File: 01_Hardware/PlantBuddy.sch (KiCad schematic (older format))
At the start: 68 parts, among them J1 SWD, Q1 AO3401, Q2 FS8205, Q3 FS8205, U1 CN301, U2 INA138, U3 LMC555xM, U4 XC6206P332MR, U5 BlueNRG-M1, U6 SHT20, U7 CN3063, U8 DW01+G, Y1 16MHz, Y2 32kHz

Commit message: PCB almost done
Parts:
- renumbered Q2 to Q3
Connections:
- net VCC: no longer C1.1, Q1.3 (D), R8.1, U3.4 (R), U3.8 (VCC)
- new net Vhum: C1.1, Q1.3 (D), R8.1, U3.4 (R), U3.8 (VCC)
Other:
- note added: "98_Other/PCB-Considerations.jpg"
- note removed: "pic/PCB-Considerations.jpg"
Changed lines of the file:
@@
 $EndComp
 Connection ~ 3675 2100
-$Comp
-L power:VCC #PWR05
-U 1 1 5F79DB75
-P 1675 1700
-F 0 "#PWR05" H 1675 1550 50  0001 C CNN
-F 1 "VCC" H 1690 1873 50  0000 C CNN
-F 2 "" H 1675 1700 50  0001 C CNN
-F 3 "" H 1675 1700 50  0001 C CNN
-	1    1675 1700
-	1    0    0    -1
-$EndComp
 Text Label 3550 1900 2    50   ~ 0
 fHumidity
@@
 Wire Wire Line
 	1675 1700 1900 1700
-Connection ~ 1675 1700
 $Comp
 L power:GND #PWR06
@@
 $EndComp
 Connection ~ 900  1000
-$Comp
-L power:VCC #PWR07
-U 1 1 5F7A3D8C
-P 1700 1000
-F 0 "#PWR07" H 1700 850 50  0001 C CNN
-F 1 "VCC" H 1715 1173 50  0000 C CNN
-F 2 "" H 1700 1000 50  0001 C CNN
-F 3 "" H 1700 1000 50  0001 C CNN
-	1    1700 1000
-	1    0    0    -1
-$EndComp
 Wire Wire Line
 	1700 1000 1500 1000
@@
 Special layout considerations:
 Text Notes 6475 775  0    50   ~ 10
-pic/PCB-Considerations.jpg
+98_Other/PCB-Considerations.jpg
 $Comp
 L Device:Antenna_Shield AE1
@@
 U 1 1 5F7C98A8
 P 5775 4325
-F 0 "R13" H 5625 4375 50  0000 L CNN
+F 0 "R13" H 5575 4375 50  0000 L CNN
 F 1 "10k" H 5575 4275 50  0000 L CNN
 F 2 "Resistor_SMD:R_0603_1608Metric" H 5775 4325 50  0001 C CNN
@@
 $EndComp
 $Comp
-L PidgeonRepeller:Q_DUAL_NMOS_FS8205 Q2
+L PidgeonRepeller:Q_DUAL_NMOS_FS8205 Q3
 U 2 1 5F8AAEF8
 P 9975 6150
-F 0 "Q2" V 10224 6150 50  0000 C CNN
+F 0 "Q3" V 10224 6150 50  0000 C CNN
 F 1 "FS8205" V 10315 6150 50  0000 C CNN
 F 2 "Package_TO_SOT_SMD:SOT-23-6" H 10175 6150 50  0001 C CNN
@@
 	2    9975 6150
 	0    1    1    0
-$EndComp
-$Comp
-L PidgeonRepeller:Q_DUAL_NMOS_FS8205 Q3
-U 1 1 5F8AC644
-P 10375 6150
-F 0 "Q3" V 10624 6150 50  0000 C CNN
-F 1 "FS8205" V 10715 6150 50  0000 C CNN
-F 2 "Package_TO_SOT_SMD:SOT-23-6" H 10575 6150 50  0001 C CNN
-F 3 "~" H 10575 6150 50  0001 C CNN
-F 4 "C32254" H 10375 6150 50  0001 C CNN "LCSC"
-	1    10375 6150
-	0    -1   1    0
 $EndComp
 Wire Wire Line
@@
 Text Notes 7800 3350 0    26   ~ 0
 RoT: ~~0.3pF per PAD
+$Comp
+L PidgeonRepeller:Q_DUAL_NMOS_FS8205 Q3
+U 1 1 5F8AC644
+P 10375 6150
+F 0 "Q3" V 10624 6150 50  0000 C CNN
+F 1 "FS8205" V 10715 6150 50  0000 C CNN
+F 2 "Package_TO_SOT_SMD:SOT-23-6" H 10575 6150 50  0001 C CNN
+F 3 "~" H 10575 6150 50  0001 C CNN
+F 4 "C32254" H 10375 6150 50  0001 C CNN "LCSC"
+	1    10375 6150
+	0    -1   1    0
+$EndComp
+Text Label 1700 1000 2    50   ~ 0
+Vhum
+Text Label 1675 1700 0    50   ~ 0
+Vhum
 $EndSCHEMATC

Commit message: Initial Layout done
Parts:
- removed C16: 100nF, Capacitor_SMD:C_0603_1608Metric, symbol Device:C_Small
- SC1: footprint TestPoint:TestPoint_2Pads_Pitch5.08mm_Drill1.3mm -> PlantBuddy:SolarCell
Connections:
- no-connect marks 5 -> 6
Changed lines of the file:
@@
 F 0 "SC1" H 1008 4621 50  0000 L CNN
 F 1 "Solar_Cell" H 1008 4530 50  0000 L CNN
-F 2 "TestPoint:TestPoint_2Pads_Pitch5.08mm_Drill1.3mm" V 900 4585 50  0001 C CNN
+F 2 "PlantBuddy:SolarCell" V 900 4585 50  0001 C CNN
 F 3 "~" V 900 4585 50  0001 C CNN
 	1    900  4525
@@
 NoConn ~ 5775 3725
 $Comp
-L Device:C_Small C16
-U 1 1 5FA07683
-P 7325 4275
-F 0 "C16" H 7450 4325 50  0000 L CNN
-F 1 "100nF" H 7425 4250 50  0000 L CNN
-F 2 "Capacitor_SMD:C_0603_1608Metric" H 7325 4275 50  0001 C CNN
-F 3 "~" H 7325 4275 50  0001 C CNN
-F 4 "C14663" H 7325 4275 50  0001 C CNN "LCSC"
-	1    7325 4275
-	1    0    0    -1
-$EndComp
-$Comp
 L Device:C_Small C9
 U 1 1 5FA07E6E
@@
 	1    0    0    -1
 $EndComp
-Wire Wire Line
-	7325 4425 7125 4425
-Connection ~ 7125 4425
-Wire Wire Line
-	7125 4125 7325 4125
-Wire Wire Line
-	7325 4425 7325 4375
-Wire Wire Line
-	7325 4175 7325 4125
 NoConn ~ 7125 4025
 Wire Wire Line
@@
 Text Label 1675 1700 0    50   ~ 0
 Vhum
+NoConn ~ 7125 4125
 $EndSCHEMATC

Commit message: Ordered PCB
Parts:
- C26: value 22pF -> 20pF; LCSC C1555 -> C1554
- D2: LCSC C72043 -> C2286
- L3: LCSC C27124 -> C77122
- R16: value 160R -> 1k; LCSC C22814 -> C21190
- R8: value Ra -> 330k; LCSC (none) -> C17629
- R9: value Rb -> 330k; LCSC (none) -> C17629
- U6: value SHT20 -> SHT21; LCSC C53865 -> C84828
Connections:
- net VCC: now also U2.4 (-); no longer U2.3 (+)
- net VPanel: now also U2.3 (+); no longer U2.4 (-)
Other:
- note added: "N3: Avoid debugging this circuit w/o battery connected."
- note added: "eN5: With 330k we get a nice \n~~1.4MHz signal for 1pF\nand a 1kHz signal at 1nF"
- note removed: "Footprint TBD"
- note removed: "N3: Never debug this circuit w/o battery connected."
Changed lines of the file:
@@
 P 3675 2200
 F 0 "R9" H 3734 2246 50  0000 L CNN
-F 1 "Rb" H 3734 2155 50  0000 L CNN
+F 1 "330k" H 3734 2155 50  0000 L CNN
 F 2 "Resistor_SMD:R_0805_2012Metric" H 3675 2200 50  0001 C CNN
 F 3 "~" H 3675 2200 50  0001 C CNN
+F 4 "C17629" H 3675 2200 50  0001 C CNN "LCSC"
 	1    3675 2200
 	1    0    0    -1
@@
 P 3675 2000
 F 0 "R8" H 3734 2046 50  0000 L CNN
-F 1 "Ra" H 3734 1955 50  0000 L CNN
+F 1 "330k" H 3734 1955 50  0000 L CNN
 F 2 "Resistor_SMD:R_0805_2012Metric" H 3675 2000 50  0001 C CNN
 F 3 "~" H 3675 2000 50  0001 C CNN
+F 4 "C17629" H 3675 2000 50  0001 C CNN "LCSC"
 	1    3675 2000
 	1    0    0    -1
@@
 P 6925 1400
 F 0 "U6" H 6750 1825 50  0000 C CNN
-F 1 "SHT20" H 6825 1750 50  0000 C CNN
+F 1 "SHT21" H 6825 1750 50  0000 C CNN
 F 2 "Package_DFN_QFN:DFN-6-1EP_3x3mm_P1mm_EP1.5x2.4mm" H 6925 1400 50  0001 C CNN
 F 3 "https://datasheet.lcsc.com/szlcsc/Sensirion-SHT20_C53865.pdf" H 6925 1400 50  0001 C CNN
-F 4 "C53865" H 6925 1400 50  0001 C CNN "LCSC"
+F 4 "C84828" H 6925 1400 50  0001 C CNN "LCSC"
 	1    6925 1400
 	1    0    0    -1
@@
 F 4 "C47914" V 2050 4350 50  0001 C CNN "LCSC"
 	1    2050 4350
-	0    1    1    0
+	0    -1   1    0
 $EndComp
 $Comp
@@
 	-1   0    0    1
 $EndComp
-Wire Wire Line
-	2050 4850 1750 4850
 Connection ~ 2050 4850
 Wire Wire Line
@@
 Wire Wire Line
 	900  4050 900  4325
-Wire Wire Line
-	1750 4250 1750 4850
 Wire Wire Line
 	2050 4650 2500 4650
@@
 L power:+3.3V #PWR08
 U 1 1 5F81D2F2
-P 2350 4250
-F 0 "#PWR08" H 2350 4100 50  0001 C CNN
-F 1 "+3.3V" H 2475 4350 50  0000 C CNN
-F 2 "" H 2350 4250 50  0001 C CNN
-F 3 "" H 2350 4250 50  0001 C CNN
-	1    2350 4250
-	1    0    0    -1
+P 1750 4250
+F 0 "#PWR08" H 1750 4100 50  0001 C CNN
+F 1 "+3.3V" H 1875 4350 50  0000 C CNN
+F 2 "" H 1750 4250 50  0001 C CNN
+F 3 "" H 1750 4250 50  0001 C CNN
+	1    1750 4250
+	-1   0    0    -1
 $EndComp
 Text Notes 2375 3975 0    50   ~ 0
@@
 U 1 1 5F88B2CB
 P 7775 5875
-F 0 "R17" H 7716 5921 50  0000 R CNN
-F 1 "120k" H 7716 5830 50  0000 R CNN
+F 0 "R17" H 7750 5925 50  0000 R CNN
+F 1 "120k" H 7750 5825 50  0000 R CNN
 F 2 "Resistor_SMD:R_0603_1608Metric" H 7775 5875 50  0001 C CNN
 F 3 "~" H 7775 5875 50  0001 C CNN
@@
 Wire Wire Line
 	7125 3225 7525 3225
-Text Notes 4300 2400 0    50   ~ 0
-Footprint TBD
 Wire Wire Line
 	9100 4875 9100 5400
@@
 	1    0    0    -1
 $EndComp
-Wire Wire Line
-	1750 4850 900  4850
-Connection ~ 1750 4850
 Connection ~ 900  4850
 $Comp
@@
 $EndComp
 Text Notes 7050 6725 0    50   ~ 0
-N3: Never debug this circuit w/o battery connected.
+N3: Avoid debugging this circuit w/o battery connected.
 $Comp
 L Device:D_Schottky_Small D1
@@
 F 2 "LED_SMD:LED_0603_1608Metric" V 7650 3800 50  0001 C CNN
 F 3 "~" V 7650 3800 50  0001 C CNN
-F 4 "C72043" V 7650 3800 50  0001 C CNN "LCSC"
+F 4 "C2286" V 7650 3800 50  0001 C CNN "LCSC"
 	1    7650 3800
 	0    -1   -1   0
@@
 P 7650 3600
 F 0 "R16" V 7454 3600 50  0000 C CNN
-F 1 "160R" V 7545 3600 50  0000 C CNN
+F 1 "1k" V 7545 3600 50  0000 C CNN
 F 2 "Resistor_SMD:R_0603_1608Metric" H 7650 3600 50  0001 C CNN
 F 3 "~" H 7650 3600 50  0001 C CNN
-F 4 "C22814" V 7650 3600 50  0001 C CNN "LCSC"
+F 4 "C21190" V 7650 3600 50  0001 C CNN "LCSC"
 	1    7650 3600
 	-1   0    0    1
@@
 F 2 "Inductor_SMD:L_0402_1005Metric" H 9075 2775 50  0001 C CNN
 F 3 "~" H 9075 2775 50  0001 C CNN
-F 4 "C27124" H 9075 2775 50  0001 C CNN "LCSC"
+F 4 "C77122" H 9075 2775 50  0001 C CNN "LCSC"
 	1    9075 2775
 	0    -1   -1   0
@@
 P 9550 2775
 F 0 "C26" V 9350 2850 50  0000 R CNN
-F 1 "22pF" V 9425 2875 50  0000 R CNN
+F 1 "20pF" V 9425 2875 50  0000 R CNN
 F 2 "Capacitor_SMD:C_0402_1005Metric" H 9550 2775 50  0001 C CNN
 F 3 "~" H 9550 2775 50  0001 C CNN
-F 4 "C1555" H 9550 2775 50  0001 C CNN "LCSC"
+F 4 "C1554" H 9550 2775 50  0001 C CNN "LCSC"
 	1    9550 2775
 	0    1    1    0
@@
 Vhum
 NoConn ~ 7125 4125
+Text Notes 3975 2175 0    50   ~ 0
+eN5: With 330k we get a nice \n~~1.4MHz signal for 1pF\nand a 1kHz signal at 1nF
+Wire Wire Line
+	900  4850 2050 4850
+$Comp
+L power:GND #PWR0101
+U 1 1 5F89C24C
+P 2350 4250
+F 0 "#PWR0101" H 2350 4000 50  0001 C CNN
+F 1 "GND" H 2355 4077 50  0000 C CNN
+F 2 "" H 2350 4250 50  0001 C CNN
+F 3 "" H 2350 4250 50  0001 C CNN
+	1    2350 4250
+	1    0    0    -1
+$EndComp
 $EndSCHEMATC

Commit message: Evrika! We have an LED blinking! 🔥🎉💯
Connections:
- net +3V3: now also U5.27 (SMPSFILT2)
- no-connect marks 6 -> 5
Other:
- note added: "E1: The maximum output swing is Vss - 1V = 2.3V\nwhich is equivalent to a current of ~~24mA.\nWe need to lower the gain by choosing\nanother resistor value. Say 330k. Do this in\nthe next iteration & solder manually at home"
- note added: "N5: !WE NEED! SMPSFILT2\nto be connected to VCC"
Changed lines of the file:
@@
 Text Label 1675 1700 0    50   ~ 0
 Vhum
-NoConn ~ 7125 4125
 Text Notes 3975 2175 0    50   ~ 0
 eN5: With 330k we get a nice \n~~1.4MHz signal for 1pF\nand a 1kHz signal at 1nF
@@
 	1    0    0    -1
 $EndComp
+Text Notes 1375 5425 0    50   ~ 0
+E1: The maximum output swing is Vss - 1V = 2.3V\nwhich is equivalent to a current of ~~24mA.\nWe need to lower the gain by choosing\nanother resistor value. Say 330k. Do this in\nthe next iteration & solder manually at home
+$Comp
+L power:+3.3V #PWR?
+U 1 1 5FA2857E
+P 7375 4125
+F 0 "#PWR?" H 7375 3975 50  0001 C CNN
+F 1 "+3.3V" H 7390 4298 50  0000 C CNN
+F 2 "" H 7375 4125 50  0001 C CNN
+F 3 "" H 7375 4125 50  0001 C CNN
+	1    7375 4125
+	1    0    0    -1
+$EndComp
+Wire Wire Line
+	7375 4125 7125 4125
+Text Notes 7300 4325 0    50   ~ 10
+N5: !WE NEED! SMPSFILT2\nto be connected to VCC
 $EndSCHEMATC

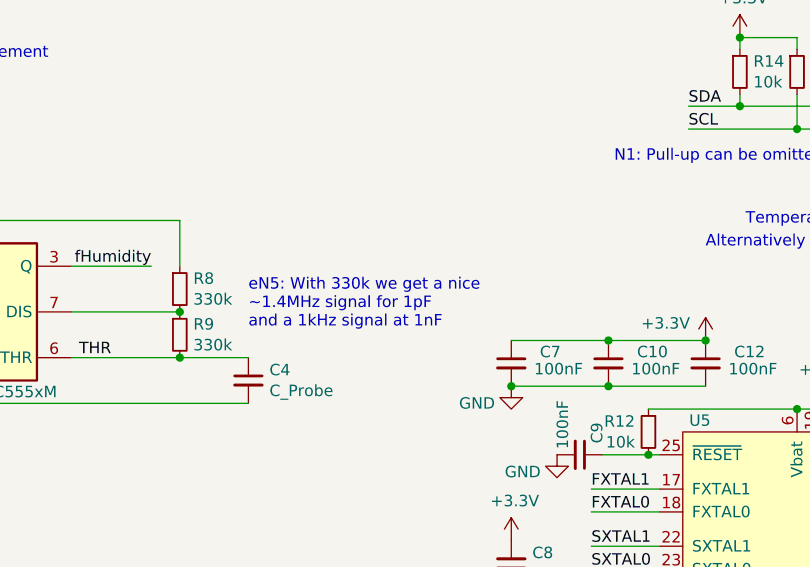
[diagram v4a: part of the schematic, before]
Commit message: Just some small typo fix.
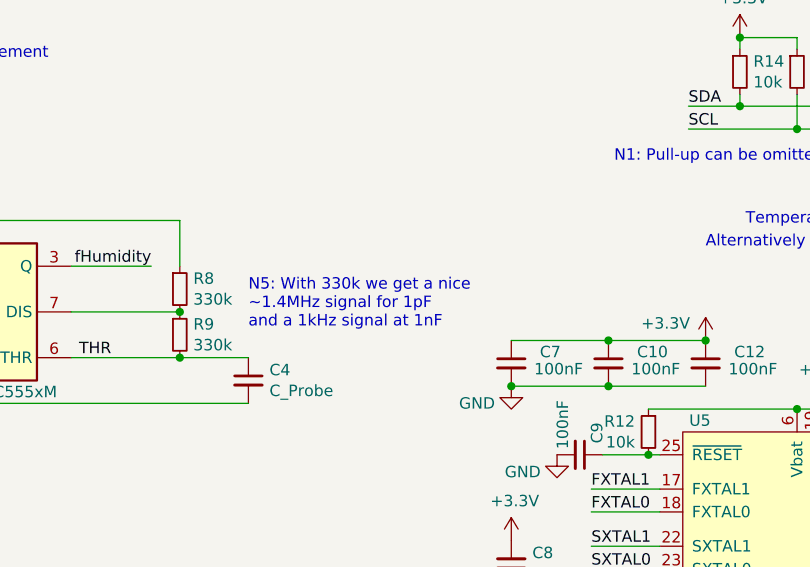
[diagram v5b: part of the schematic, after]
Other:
- note added: "N5: With 330k we get a nice \n~~1.4MHz signal for 1pF\nand a 1kHz signal at 1nF"
- note removed: "eN5: With 330k we get a nice \n~~1.4MHz signal for 1pF\nand a 1kHz signal at 1nF"
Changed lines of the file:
@@
 Vhum
 Text Notes 3975 2175 0    50   ~ 0
-eN5: With 330k we get a nice \n~~1.4MHz signal for 1pF\nand a 1kHz signal at 1nF
+N5: With 330k we get a nice \n~~1.4MHz signal for 1pF\nand a 1kHz signal at 1nF
 Wire Wire Line
 	900  4850 2050 4850

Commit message: Started schematic revision
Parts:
- removed BT1: Li+, Battery:BatteryHolder_Keystone_1060_1x2032, symbol Device:Battery_Cell
- removed C17, C21, C25: 22uF, Capacitor_SMD:C_0603_1608Metric, symbol Device:C_Small
- removed C24: 100nF, Capacitor_SMD:C_0603_1608Metric, symbol Device:C_Small
- removed C3, C5: 2.2uF, Capacitor_SMD:C_0603_1608Metric, symbol Device:C_Small
- removed D1, D3: B5819W, Diode_SMD:D_SOD-123, symbol Device:D_Schottky_Small
- removed Q2, Q3: FS8205, Package_TO_SOT_SMD:SOT-23-6, symbol PidgeonRepeller:Q_DUAL_NMOS_FS8205
- removed R1, R3, R4: 1M, Resistor_SMD:R_0603_1608Metric, symbol Device:R_Small
- removed R10, R11, R17: 120k, Resistor_SMD:R_0603_1608Metric, symbol Device:R_Small
- removed R18: 160R, Resistor_SMD:R_0603_1608Metric, symbol Device:R_Small
- removed R19, R7: 10k, Resistor_SMD:R_0603_1608Metric, symbol Device:R_Small
- removed R5: 1R0, Resistor_SMD:R_0603_1608Metric, symbol Device:R_Small
- removed R6: 470k, Resistor_SMD:R_0603_1608Metric, symbol Device:R_Small
- removed SC1: Solar_Cell, PlantBuddy:SolarCell, symbol Device:Solar_Cell
- removed U1: CN301, Package_TO_SOT_SMD:SOT-23-5, symbol PlantBuddy:CN301
- removed U2: INA138, Package_TO_SOT_SMD:SOT-23-5, symbol Amplifier_Current:INA138
- removed U4: XC6206P332MR, Package_TO_SOT_SMD:SOT-23, symbol Regulator_Linear:MCP1700-3302E_SOT23
- removed U7: CN3063, Package_SO:SOP-8_3.9x4.9mm_P1.27mm, symbol PlantBuddy:CN3063
- removed U8: DW01+G, Package_TO_SOT_SMD:SOT-23-6, symbol PidgeonRepeller:DW01+G
- added BT?: Li+, Battery:BatteryHolder_Keystone_1060_1x2032, symbol Device:Battery_Cell
- added C?: 100nF, Capacitor_SMD:C_0402_1005Metric, symbol Device:C_Small
- added C?: 1uF, Capacitor_SMD:C_0402_1005Metric, symbol Device:C_Small
- added L?: 10uH, Inductor_SMD:L_0805_2012Metric, symbol Device:L_Small
- added U?: LTR-303ALS-01, OptoDevice:Lite-On_LTR-303ALS-01, symbol Sensor_Optical:LTR-303ALS-01
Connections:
- net +BATT: now also C10.1, C12.1, C15.1, C7.1, C8.2, J1.1 (Pin_1), Q1.2 (S), R12.1, R14.1, R15.1, R2.1, U5.19 (Vbat), U5.24 (Vbat), U5.6 (Vbat), U6.5 (VDD), BT?.1 (+), U?.1 (VDD)
- net SCL: now also U?.4 (SCL)
- net SDA: now also U?.6 (SDA)
- net at U5.26 (SMPSFILT1): now also L?.1
- removed net +3V3: C10.1, C12.1, C15.1, C7.1, C8.2, Q1.2 (S), R12.1, R14.1, R15.1, R2.1, U5.19 (Vbat), U5.24 (Vbat), U5.27 (SMPSFILT2), U5.6 (Vbat), U6.5 (VDD)
- net -BATT renamed GND
- net GND: now also BT?.2 (-), C?.2, C?.2, U?.3 (GND)
- net ADC1: no longer names the net of U5.15 (ADC1)
- net IRR_EN renamed LUX_INT
- net LUX_INT: now also U?.5 (INT)
- net Vhum: no longer names the net of C1.1, Q1.3 (D), R8.1, U3.4 (R), U3.8 (VCC)
- net ~CHG_DONE: no longer names the net of U5.9 (IO3)
- net ~CHG_ON: no longer names the net of U5.10 (IO2)
- net ~HEN~ renamed ~SOIL_EN~
- net ~LBO_ISR: no longer names the net of U5.7 (IO5)
- new net: C?.1, C?.1, L?.2, U5.27 (SMPSFILT2)
- no-connect marks 5 -> 6
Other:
- note added: "0 to 65535 Lux Light sensor"
- note added: "ADC can be configured to\ninternally sense VBat"
- note added: "Added SMPS\nfor minimum\npower"
- note added: "N3: DO NOT debug with battery connected!"
- note added: "N5: The free-air capacitance is 46pF\nyielding a free-air frequency of 30kHz\nTo-Do:\nChange to 10k so that\nf_air = 0.7MHz"
- note added: "Put it in such a way that\n it is small and hidden\nWe will need to build \na programming rig for it!"
- note added: "Should I put 0402\nor leave 0805?"
- note added: "TODO: Replace with the MUCH cheaper SHTC3"
- note removed: "15mA max\nchg. current\n(~~1/3C)"
- note removed: "2.82V @ 30mA"
- note removed: "3.3V 1uA Iq LDO"
- note removed: "Battery protection using DW01"
- note removed: "CR2032-BS-6-1"
- note removed: "E1: The maximum output swing is Vss - 1V = 2.3V\nwhich is equivalent to a current of ~~24mA.\nWe need to lower the gain by choosing\nanother resistor value. Say 330k. Do this in\nthe next iteration & solder manually at home"
- note removed: "G=94"
- note removed: "N3: Avoid debugging this circuit w/o battery connected."
- note removed: "N5: !WE NEED! SMPSFILT2\nto be connected to VCC"
- note removed: "N5: With 330k we get a nice \n~~1.4MHz signal for 1pF\nand a 1kHz signal at 1nF"
- note removed: "To Load"
- note removed: "To uC"
- note removed: "Use CN301 as Low Battery Indicator (3.4V) &\nPut all devices to sleep until battery is charged"
- note removed: "We need to be able to short circuit the panel\nso that we can measure the solar irradiance\nsince these two values are linearly dependent"
- note removed: "We use CN3063 as a simpler, lower part count solution\nto the CN3791"
- note removed: "~~30mA max"
- note removed: "~~5uA leakage @ 25 °C"
- moved on the sheet: C15, D2, J1, Q1, R14, R15, R16, R2, U6

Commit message: Revised schematic
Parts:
- removed C15: 100nF, Capacitor_SMD:C_0603_1608Metric, symbol Device:C_Small
- removed U6: SHT21, Package_DFN_QFN:DFN-6-1EP_3x3mm_P1mm_EP1.5x2.4mm, symbol PlantBuddy:SHT20
- removed U?: LTR-303ALS-01, OptoDevice:Lite-On_LTR-303ALS-01, symbol Sensor_Optical:LTR-303ALS-01
- added C3: 100nF, Capacitor_SMD:C_0402_1005Metric, symbol Device:C_Small
- added D1: Y, LED_SMD:LED_0603_1608Metric, symbol Device:LED_Small
- added J2: Conn_I2C_SDA, TestPoint:TestPoint_Pad_D1.5mm, symbol Connector_Generic:Conn_01x01
- added J3: Conn_I2C_SCL, TestPoint:TestPoint_Pad_D1.5mm, symbol Connector_Generic:Conn_01x01
- added Q2: AO3400A, Package_TO_SOT_SMD:SOT-23, symbol Device:Q_NMOS_GSD
- added R1: 10k, Resistor_SMD:R_0402_1005Metric, symbol Device:R_Small
- added R3: 1k, Resistor_SMD:R_0402_1005Metric, symbol Device:R_Small
- added SW1: PWR_SW, Button_Switch_SMD:SW_SPDT_CK-JS102011SAQN, symbol Switch:SW_SPDT
- added SW2: BLE_RST_SW, Button_Switch_SMD:SW_SPST_EVQP7C, symbol Switch:SW_Push
- added U1: OPT3001, PlantBuddy:OPT3001DNPR, symbol PlantBuddy:OPT3001
- added U6: SHTC3, PlantBuddy:Sensirion_DFN-4-1EP_2x2mm_P1mm_EP0.7x1.6mm, symbol Sensor_Humidity:SHTC3
- BT1: renamed from BT?; footprint Battery:BatteryHolder_Keystone_1060_1x2032 -> PlantBuddy:BatteryHolder_LCSC_2032
- C1, C10, C12, C2, C7, C9: footprint Capacitor_SMD:C_0603_1608Metric -> Capacitor_SMD:C_0402_1005Metric; LCSC C14663 -> C1525
- D2: value Status -> R
- J1: footprint Connector_JST:JST_SH_BM04B-SRSS-TB_1x04-1MP_P1.00mm_Vertical -> PlantBuddy:Debug_Connector; LCSC (none) -> C541879
- R12, R13, R14, R15, R2: footprint Resistor_SMD:R_0603_1608Metric -> Resistor_SMD:R_0402_1005Metric; LCSC C25804 -> C25744
- R16: footprint Resistor_SMD:R_0603_1608Metric -> Resistor_SMD:R_0402_1005Metric; LCSC C21190 -> C11702
- R8, R9: value 330k -> 10k; footprint Resistor_SMD:R_0805_2012Metric -> Resistor_SMD:R_0402_1005Metric; LCSC C17629 -> C25744
- gave numbers to parts that had none: 3
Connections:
- net +BATT: now also C3.1, R1.1, SW1.3 (C), U1.1 (VDD), U6.1 (VDD); no longer BT1.1 (+)
- net GND: now also C3.2, D1.1 (K), Q2.2 (S), SW2.2, U1.2 (ADDR), U1.3 (GND), U1.7 (PAD), U6.4 (VSS); no longer BT1.2 (-)
- net LUX_INT: now also U1.5 (INT)
- net SCL: now also R14.2, J3.1 (Pin_1), U1.4 (SCL), U6.2 (SCL); no longer R15.2
- net SDA: now also R15.2, J2.1 (Pin_1), U1.6 (SDA), U6.3 (SDA); no longer R14.2
- net ~BLE_RST: now reaches U5.7 (IO5)
- net ~BLE_RST: now also R1.2, SW2.1
- net LEDY: now reaches U5.9 (IO3)
- net LEDY: now also R3.2
- net LED renamed LEDR
- new net: D1.2 (A), R3.1
- new net: BT1.1 (+), Q2.1 (G), SW1.2 (B)
- new net: BT1.2 (-), Q2.3 (D)
- no-connect marks 6 -> 7
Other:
- note added: "0 to 83865 Lux Light sensor"
- note added: "A really small cheap button to be used\nfor resetting the bluetooth connection\nor reset to default settings"
- note added: "Impedance matching to 25.4Ω\nby subtracting imaginary part\n"
- note added: "Low-power reverse voltage protection\n& shutdown switch"
- note added: "N5: The free-air capacitance is 46pF\nyielding a free-air frequency of 700kHz"
- note added: "Reverse-voltage protection"
- note added: "Temperature & Humidity\nReally cheap: 0.66$"
- note added: "Yellow status LED => short blinks\nto notify user of different actions"
- note removed: "0 to 65535 Lux Light sensor"
- note removed: "98_Other/PCB-Considerations.jpg"
- note removed: "Alternatively use SHT21 (C84828)"
- note removed: "Impedance matching to 25.4Ω\n"
- note removed: "N1: Pull-up can be omitted"
- note removed: "N5: The free-air capacitance is 46pF\nyielding a free-air frequency of 30kHz\nTo-Do:\nChange to 10k so that\nf_air = 0.7MHz"
- note removed: "Special layout considerations:"
- note removed: "TODO: Replace with the MUCH cheaper SHTC3"
- note removed: "Temperature & Humidity"
- moved on the sheet: BT1, R14, R15

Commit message: Ordered PCB version 2
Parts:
- U1: footprint PlantBuddy:OPT3001DNPR -> Package_DFN_QFN:DFN-6-1EP_2x2mm_P0.65mm_EP1x1.6mm
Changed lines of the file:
@@
 F 0 "U1" H 1375 7396 50  0000 C CNN
 F 1 "OPT3001" H 1575 7075 50  0000 C CNN
-F 2 "PlantBuddy:OPT3001DNPR" H 1375 6375 50  0001 C CNN
+F 2 "Package_DFN_QFN:DFN-6-1EP_2x2mm_P0.65mm_EP1x1.6mm" H 1375 6375 50  0001 C CNN
 F 3 "https://www.ti.com/lit/ds/symlink/opt3001.pdf" H 1375 6375 50  0001 C CNN
 F 4 "C90462" H 1575 6450 50  0001 C CNN "LCSC"
